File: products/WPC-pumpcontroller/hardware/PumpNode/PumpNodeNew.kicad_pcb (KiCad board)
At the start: 2 copper layers, 83 x 72 mm, 45 parts, among them J1 Conn_IN, J2 Conn_Coaxial_Small, J3 PWR_CONN, J4 Relay_CONN, K1 Cube_Relay, U1 ULN2003, U13 AMS1117-5.0, U5 ESP32 30 Pin CP2102 Developme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, U7 ISC-SX1262-B, U8 AP2112K-3.3

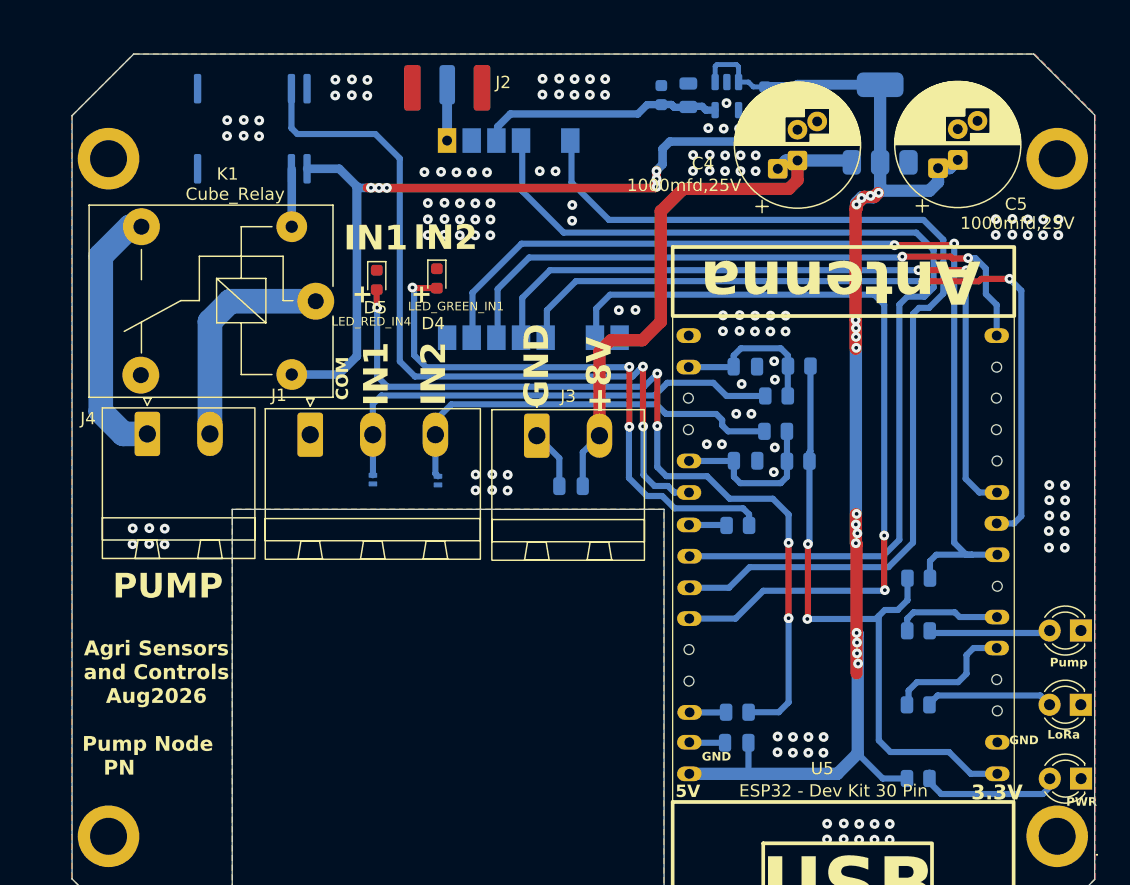
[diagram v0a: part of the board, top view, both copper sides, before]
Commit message: WPC: PumpNode + WPC board updates, add 2x panel and Gerber exports
- Update PumpNode and WPC KiCad PCB/schematic/project-local files
- Add WPC-panel2x (2-up panelized PumpNode layout) KiCad project
- Add Gerber/drill export sets for PumpNode and the 2x panel

Co-Authored-By: Claude Sonnet 5 <noreply@anthropic.com>
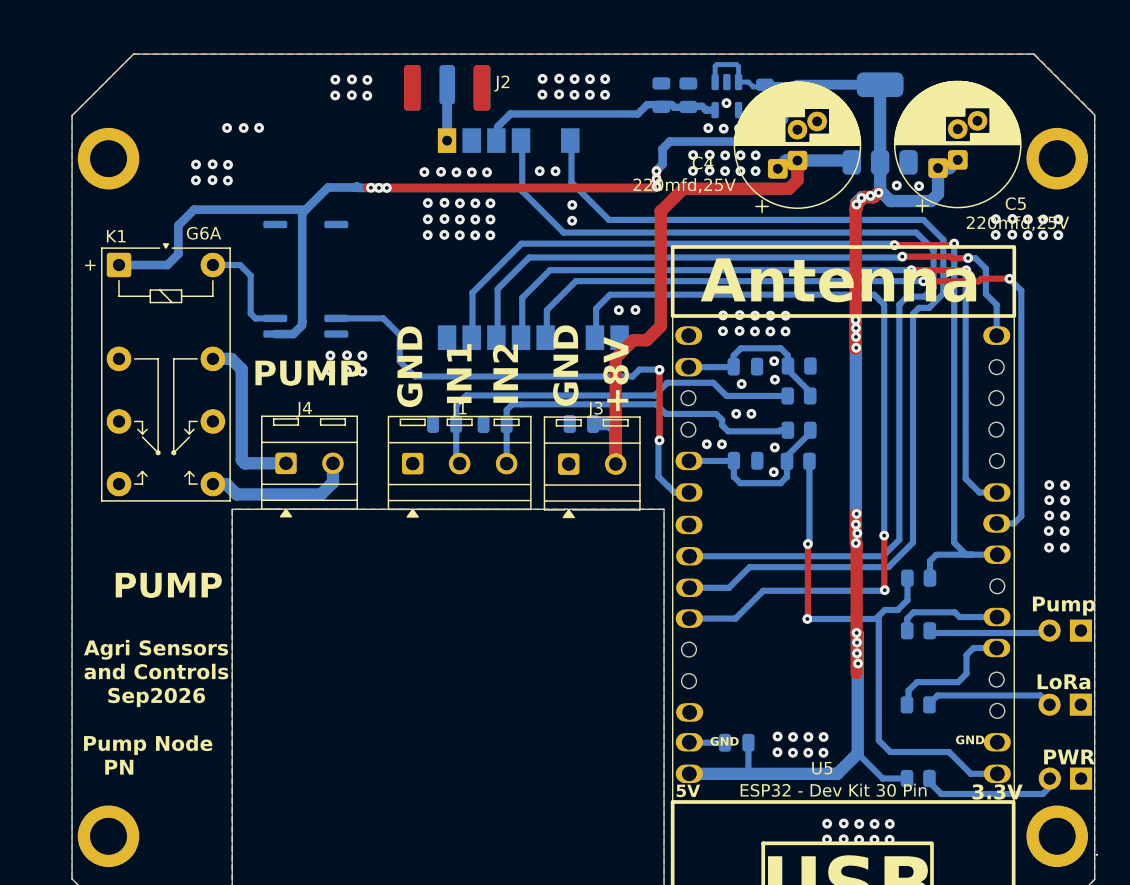
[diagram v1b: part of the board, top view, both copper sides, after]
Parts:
- removed D4: LED_GREEN_IN1, LED_SMD:LED_0603_1608Metric
- removed D5: LED_RED_IN4, LED_SMD:LED_0603_1608Metric
- removed R6, R8: 470E, Resistor_SMD:R_0805_2012Metric
- C10, C12: value 10mfd,10V tentalum -> 10mfd,10V tent; footprint Capacitor_SMD:C_0603_1608Metric -> Capacitor_SMD:C_0805_2012Metric
- C4, C5: value 1000mfd,25V -> 220mfd,25V
- D6, D7: value PESD3V3U1UL -> PESD; footprint Diode_SMD:D_SOD-882 -> Diode_SMD:D_0805_2012Metric
- J1: footprint Connector_Phoenix_MSTB:PhoenixContact_MSTBA_2,5_3-G-5,08_1x03_P5.08mm_Horizontal -> TerminalBlock_MetzConnect:TerminalBlock_MetzConnect_Type086_RT03403HBLC_1x03_P3.81mm_Horizontal
- J3, J4: footprint Connector_Phoenix_MSTB:PhoenixContact_MSTBA_2,5_2-G-5,08_1x02_P5.08mm_Horizontal -> TerminalBlock_MetzConnect:TerminalBlock_MetzConnect_Type086_RT03402HBLC_1x02_P3.81mm_Horizontal
- K1: value Cube_Relay -> G6A; footprint Relay_THT:Relay_SPDT_SANYOU_SRD_Series_Form_C -> Relay_THT:Relay_DPDT_Omron_G6A
- R1: value 470E -> 2K2
- U1: footprint Package_SO:SOIC-16W_5.3x10.2mm_P1.27mm -> Package_SO:SOIC-16_3.9x9.9mm_P1.27mm
- moved K1 16.2 mm to (157.7, 66.8), turned to 0 degrees
- moved U1 13.0 mm to (172.8, 67.9), turned to 180 degrees
- moved J4 11.5 mm to (171.2, 82.9)
- moved J1 8.64 mm to (181.5, 82.9)
- moved D6 7.35 mm to (184.1, 79.7), turned to 180 degrees
- moved D7 6.51 mm to (188.2, 79.7), turned to 180 degrees
- moved C6 5.11 mm to (195.2, 79.7)
- moved J3 3.47 mm to (194.2, 82.9)
- moved R11 1.90 mm to (212.9, 80.2)
- moved R9 1.82 mm to (212.9, 77.4)
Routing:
- net Net-(D5-A): track 69.3 -> 0.00 mm, vias 5 -> 0
- net Net-(D4-A): track 46.5 -> 0.00 mm, vias 3 -> 0
- net /RELAY1_MCU: track 63.2 -> 41.4 mm
- net +5V: track 185.6 -> 194.2 mm
- net +3.3V: track 52.3 -> 44.6 mm
- net /RLY_COMM: track 21.4 -> 13.8 mm
- net /RL1_CON_1: track 18.4 -> 12.1 mm
- net /IN1_CON: track 38.8 -> 32.9 mm
- net GND: track 7.77 -> 2.92 mm, vias 132 -> 133
- net /IN4_CON: track 33.1 -> 28.6 mm
- net /RELAY1_COIL: track 4.71 -> 8.67 mm
- net /IN1_LED_MCU: track 3.13 -> 0.06 mm
- net /IN4_LED_MCU: track 3.07 -> 0.00 mm
- net +8V: track 46.5 -> 47.6 mm
- net /IN4_MCU: track 13.4 -> 14.3 mm
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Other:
- board text added: "Agri Sensors and Controls Sep2026"
- board text added: "LoRa(B)"
- board text added: "PUMP Node PN"
- board text added: "PUMP(Y)"
- board text added: "PWR(G)"
- board text removed: "Agri Sensors and Controls Aug2026"
- board text removed: "COM"
- board text removed: "PUMP Node-PN"

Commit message: WPC: update PumpNode/WPC/WPC-panel2x boards, regenerate fab outputs
- Update PumpNode, WPC, and WPC-panel2x KiCad PCB/schematic/project-local
  files
- Regenerate Gerber/drill exports for all three boards
- Add a separate fab_output/ Gerber set for WPC-panel2x alongside its
  existing GERBER-FLOW/ export
- Replace the old PumpNode/WPC-panel2x fab zip archives with freshly
  regenerated ones

Co-Authored-By: Claude Sonnet 5 <noreply@anthropic.com>
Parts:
- removed the . at (233.8, 113.1)
- removed the ? at (156.8, 58.1)
- removed the ? at (233.8, 58.1)
- removed the ? at (156.8, 113.1)
- removed the C10 at (210.1, 53.1)
- removed the C12 at (201.7, 53.0)
- removed the C13 at (203.9, 53.0)
- removed the C3 at (208.5, 75.0)
- removed C4, C5: 220mfd,25V, Capacitor_THT:CP_Radial_D10.0mm_P2.50mm_P5.00mm
- removed the C6 at (195.2, 79.7)
- removed the C7 at (207.8, 105.6)
- removed the C8 at (208.5, 82.7)
- removed the D1 at (235.8, 108.5)
- removed the D2 at (235.8, 102.5)
- removed the D3 at (235.8, 96.4)
- removed the D6 at (184.1, 79.7)
- removed the D7 at (188.2, 79.7)
- removed H1: MountingHole, MountingHole:MountingHole_3.2mm_M3
- removed the J1 at (181.5, 82.9)
- removed the J2 at (184.3, 52.1)
- removed the J3 at (194.2, 82.9)
- removed the J4 at (171.2, 82.9)
- removed the K1 at (157.7, 66.8)
- removed the R1 at (222.6, 108.5)
- removed the R11 at (212.9, 80.2)
- removed the R12 at (212.8, 82.7)
- removed the R13 at (222.6, 92.2)
- removed the R2 at (222.6, 102.5)
- removed the R5 at (222.6, 96.5)
- removed the R7 at (212.9, 75.0)
- removed the R9 at (212.9, 77.4)
- removed the U1 at (172.8, 67.9)
- removed the U13 at (219.5, 55.3)
- removed the U5 at (229.0, 108.1)
- removed the U7 at (191.3, 64.7)
- removed the U8 at (207.0, 53.1)
- added .: MountingHole, MountingHole:MountingHole_3.2mm_M3, F.Cu at (196.1, 116.3)
- added .: MountingHole, MountingHole:MountingHole_3.2mm_M3, F.Cu at (108.3, 61.2)
- added ?: , , F.Cu at (196.1, 61.3)
- added ?: , , F.Cu at (108.3, 116.2)
- added C10: 10mfd,10V tent, Capacitor_SMD:C_0805_2012Metric, B.Cu at (108.5, 104.4)
- added C10: 10mfd,10V tent, Capacitor_SMD:C_0805_2012Metric, B.Cu at (196.0, 73.1)
- added C12: 10mfd,10V tent, Capacitor_SMD:C_0805_2012Metric, B.Cu at (112.7, 110.7)
- added C12: 10mfd,10V tent, Capacitor_SMD:C_0805_2012Metric, B.Cu at (191.7, 66.8)
- added C13: 100nF, Capacitor_SMD:C_0805_2012Metric, B.Cu at (191.6, 64.4)
- added C13: 100nF, Capacitor_SMD:C_0805_2012Metric, B.Cu at (112.8, 113.1)
- added C3: 100pF, Capacitor_SMD:C_0805_2012Metric, B.Cu at (170.3, 78.1)
- added C3: 100pF, Capacitor_SMD:C_0805_2012Metric, B.Cu at (134.1, 99.5)
- added C6: 100nF, Capacitor_SMD:C_0805_2012Metric, B.Cu at (161.5, 111.3)
- added C6: 100nF, Capacitor_SMD:C_0805_2012Metric, B.Cu at (143.0, 66.2)
- added C7: 100nF, Capacitor_SMD:C_0805_2012Metric, B.Cu at (196.0, 75.7)
- added C7: 100nF, Capacitor_SMD:C_0805_2012Metric, B.Cu at (108.5, 101.8)
- added C8: 100pF, Capacitor_SMD:C_0805_2012Metric, B.Cu at (170.4, 86.0)
- added C8: 100pF, Capacitor_SMD:C_0805_2012Metric, B.Cu at (134.1, 91.5)
- added D1: Power_Green_LED, LED_THT:LED_D3.0mm, F.Cu at (198.0, 111.6)
- added D1: Power_Green_LED, LED_THT:LED_D3.0mm, F.Cu at (106.4, 65.9)
- added D2: LED_Blue_LoRa, LED_THT:LED_D3.0mm, F.Cu at (106.4, 71.9)
- added D2: LED_Blue_LoRa, LED_THT:LED_D3.0mm, F.Cu at (198.0, 105.6)
- added D3: LED_YELLOW_PUMP, LED_THT:LED_D3.0mm, F.Cu at (198.0, 99.6)
- added D3: LED_YELLOW_PUMP, LED_THT:LED_D3.0mm, F.Cu at (106.4, 77.9)
- added D6: PESD, Diode_SMD:D_0805_2012Metric, B.Cu at (155.0, 97.9)
- added D6: PESD, Diode_SMD:D_0805_2012Metric, B.Cu at (149.4, 79.7)
- added D7: PESD, Diode_SMD:D_0805_2012Metric, B.Cu at (155.0, 104.9)
- added D7: PESD, Diode_SMD:D_0805_2012Metric, B.Cu at (149.4, 72.7)
- added J1: Conn_IN, TerminalBlock_MetzConnect:TerminalBlock_MetzConnect_Type086_RT03403HBLC_1x03_P3.81mm_Horizontal, F.Cu at (157.6, 97.3)
- added J1: Conn_IN, TerminalBlock_MetzConnect:TerminalBlock_MetzConnect_Type086_RT03403HBLC_1x03_P3.81mm_Horizontal, F.Cu at (146.8, 80.2)
- added J2: Conn_Coaxial_Small, Connector_Coaxial:SMA_Samtec_SMA-J-P-H-ST-EM1_EdgeMount, B.Cu at (162.0, 54.9)
- added J2: Conn_Coaxial_Small, Connector_Coaxial:SMA_Samtec_SMA-J-P-H-ST-EM1_EdgeMount, B.Cu at (142.5, 122.6)
- added J3: PWR_CONN, TerminalBlock_MetzConnect:TerminalBlock_MetzConnect_Type086_RT03402HBLC_1x02_P3.81mm_Horizontal, F.Cu at (146.8, 67.8)
- added J3: PWR_CONN, TerminalBlock_MetzConnect:TerminalBlock_MetzConnect_Type086_RT03402HBLC_1x02_P3.81mm_Horizontal, F.Cu at (157.6, 109.7)
- added J4: Relay_CONN, TerminalBlock_MetzConnect:TerminalBlock_MetzConnect_Type086_RT03402HBLC_1x02_P3.81mm_Horizontal, F.Cu at (147.0, 89.2)
- added J4: Relay_CONN, TerminalBlock_MetzConnect:TerminalBlock_MetzConnect_Type086_RT03402HBLC_1x02_P3.81mm_Horizontal, F.Cu at (157.4, 88.3)
- added K1: G6A, Relay_THT:Relay_DPDT_Omron_G6A, F.Cu at (149.6, 112.1)
- added K1: G6A, Relay_THT:Relay_DPDT_Omron_G6A, F.Cu at (154.9, 65.4)
- added R1: 2K2, Resistor_SMD:R_0805_2012Metric, B.Cu at (188.1, 111.6)
- added R1: 2K2, Resistor_SMD:R_0805_2012Metric, B.Cu at (116.4, 65.9)
- added R11: 470E, Resistor_SMD:R_0805_2012Metric, B.Cu at (161.6, 104.9)
- added R11: 470E, Resistor_SMD:R_0805_2012Metric, B.Cu at (142.8, 72.7)
- added R12: 10K, Resistor_SMD:R_0805_2012Metric, B.Cu at (134.1, 94.3)
- added R12: 10K, Resistor_SMD:R_0805_2012Metric, B.Cu at (170.4, 83.2)
- added R13: 10K, Resistor_SMD:R_0805_2012Metric, B.Cu at (117.0, 85.5)
- added R13: 10K, Resistor_SMD:R_0805_2012Metric, B.Cu at (187.4, 92.1)
- added R2: 470E, Resistor_SMD:R_0805_2012Metric, B.Cu at (108.5, 83.0)
- added R2: 470E, Resistor_SMD:R_0805_2012Metric, B.Cu at (196.0, 94.5)
- added R5: 470E, Resistor_SMD:R_0805_2012Metric, B.Cu at (108.5, 85.6)
- added R5: 470E, Resistor_SMD:R_0805_2012Metric, B.Cu at (196.0, 91.9)
- added R7: 10K, Resistor_SMD:R_0805_2012Metric, B.Cu at (134.1, 96.9)
- added R7: 10K, Resistor_SMD:R_0805_2012Metric, B.Cu at (170.4, 80.6)
- added R9: 470E, Resistor_SMD:R_0805_2012Metric, B.Cu at (143.0, 79.7)
- added R9: 470E, Resistor_SMD:R_0805_2012Metric, B.Cu at (161.5, 97.9)
- added U1: ULN2003, Package_SO:SOIC-16_3.9x9.9mm_P1.27mm, B.Cu at (127.6, 95.8)
- added U1: ULN2003, Package_SO:SOIC-16_3.9x9.9mm_P1.27mm, B.Cu at (176.8, 81.7)
- added U13: AMS1117-5.0, Package_TO_SOT_SMD:SOT-223-3_TabPin2, B.Cu at (174.4, 118.1)
- added U13: AMS1117-5.0, Package_TO_SOT_SMD:SOT-223-3_TabPin2, B.Cu at (130.1, 59.4)
- added U5: ESP32 30 Pin CP2102 Development Board, PCM_Espressif:ESP32-C3-DevKitM-1, F.Cu at (113.0, 67.6)
- added U5: ESP32 30 Pin CP2102 Development Board, PCM_Espressif:ESP32-C3-DevKitM-1, F.Cu at (191.5, 109.9)
- added U7: ISC-SX1262-B, RF_Module:Ai-Thinker-Ra-01-LoRa, B.Cu at (177.8, 63.6)
- added U7: ISC-SX1262-B, RF_Module:Ai-Thinker-Ra-01-LoRa, B.Cu at (126.6, 114.0)
- added U8: AP2112K-3.3, Package_TO_SOT_SMD:SOT-23-5, B.Cu at (110.7, 108.0)
- added U8: AP2112K-3.3, Package_TO_SOT_SMD:SOT-23-5, B.Cu at (193.8, 69.5)
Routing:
- net +5V: track 194.2 -> 295.9 mm, vias 22 -> 28
- net +3.3V: track 44.6 -> 93.7 mm, vias 2 -> 4
- net /IN4_MCU: track 14.3 -> 63.3 mm
- net /RELAY1_COIL: track 8.67 -> 53.9 mm
- net +3.3VL: track 19.9 -> 64.9 mm
- net /IN1_MCU: track 13.7 -> 57.1 mm
- net /NSS: track 77.8 -> 105.4 mm, vias 2 -> 0
- net /DIO1: track 81.1 -> 107.3 mm, vias 0 -> 4
- net Net-(J2-In): track 4.01 -> 29.5 mm
- net /RESET: track 82.4 -> 106.9 mm, vias 0 -> 4
- net /RLY_COMM: track 13.8 -> 38.0 mm
- net Net-(D2-A): track 10.4 -> 27.4 mm
- net /BUSY: track 66.7 -> 82.0 mm, vias 2 -> 0
- net /IN4_CON: track 28.6 -> 14.6 mm
- net +8V: track 47.6 -> 33.8 mm
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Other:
- board size 83 x 72 mm -> 93.8 x 72.1 mm
- board text added: "G"
- board text added: "I1"
- board text added: "I2"
- board text added: "J2"
- board text added: "PCB Edge"
- board text removed: "IN1"
- board text removed: "IN2"

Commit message: Workshop labs page at /workshop, GPSIOAM workshop materials, pending WIP
- agrisense-webapp: public, no-login /workshop route (middleware allowlist +
  next.config.ts rewrite) serving the student labs page from public/workshop
- docs/workshops/gpsioam-2026: 4 Wokwi-ready ESP32 labs + Lab 4 reference
  solution, labs page template and build_site.py
- Pending work committed as-is: WM2 SolarNode/WaterMaster KiCad, WPC Pump
  Node Gerbers, FG1 flash tools, marketing video projects
- .gitignore: Next.js cache, *.tsbuildinfo, KiCad *.lck, .claude/settings.local.json;
  stop tracking .next/cache

Co-Authored-By: Claude Opus 5.5 <noreply@anthropic.com>
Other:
- outline, holes or cut-outs redrawn
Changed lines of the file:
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@@
 	)
 	(gr_line
-		(start 151.4275 92.915)
-		(end 153.01 92.915)
-		(stroke
-			(width 0.05)
-			(type default)
-		)
-		(layer "Edge.Cuts")
-	)
-	(gr_line
-		(start 151.4275 92.915)
-		(end 151.4275 124.72)
+		(start 151.4275 98.61)
+		(end 153.01 98.61)
 		(stroke
 			(width 0.05)
@@
 		(start 164.1825 124.805)
 		(end 164.1825 116.415)
+		(stroke
+			(width 0.05)
+			(type default)
+		)
+		(layer "Edge.Cuts")
+	)
+	(gr_line
+		(start 153.0125 116.415)
+		(end 153.0125 98.61)
 		(stroke
 			(width 0.05)
@@
 	(gr_line
 		(start 110.2575 124.72)
+		(end 151.4275 124.72)
+		(stroke
+			(width 0.05)
+			(type default)
+		)
+		(layer "Edge.Cuts")
+	)
+	(gr_line
+		(start 151.4275 98.61)
 		(end 151.4275 124.72)
 		(stroke
@@
 		(stroke
 			(width 0.05)
-			(type default)
-		)
-		(layer "Edge.Cuts")
-	)
-	(gr_line
-		(start 153.0125 116.415)
-		(end 153.0125 92.915)
-		(stroke
-			(width 0.05)
